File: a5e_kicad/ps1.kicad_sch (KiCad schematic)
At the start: 59 parts, among them U1201 MPM54304GMN-0000, U1303 MPM3810AGQB

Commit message: add vias to lppdr balls
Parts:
- renumbered C1212 to C157, C1208 to C158, C1209 to C159, C1362 to C160, C1211 to C161, C1361 to C162, C1210 to C163, C1213 to C164, C1214 to C165, C1360 to C166, C1215 to C167, C1359 to C168, C1216 to C169, C1363 to C170, C1364 to C171, C1365 to C172, C1366 to C173, C1367 to C174, C1368 to C175, C1369 to C176, C1370 to C177, C1371 to C178, C1372 to C179, C1373 to C180, C1374 to C181, C1375 to C182, C1376 to C183, C1377 to C184, C1378 to C185, C1379 to C186, C1380 to C187, C1381 to C188, C1382 to C189, C1383 to C190, C1384 to C191, C1385 to C192, C1386 to C193, C1387 to C194, C1388 to C195, C1389 to C196, C1390 to C197, R1312 to R64, R1311 to R65, R1308 to R66, R1307 to R67, R1309 to R68, R1310 to R69, R1216 to R70, R1208 to R71, R1209 to R72, R1210 to R73, R1211 to R74, R1313 to R75, R1212 to R76, R1213 to R77, R1214 to R78, R1215 to R79, U1201 to U16, U1303 to U17

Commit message: add comments
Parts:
- added U18, U19, U8: AP61202Z6, Package_TO_SOT_SMD:SOT-563, symbol Regulator_Switching:AP61202Z6

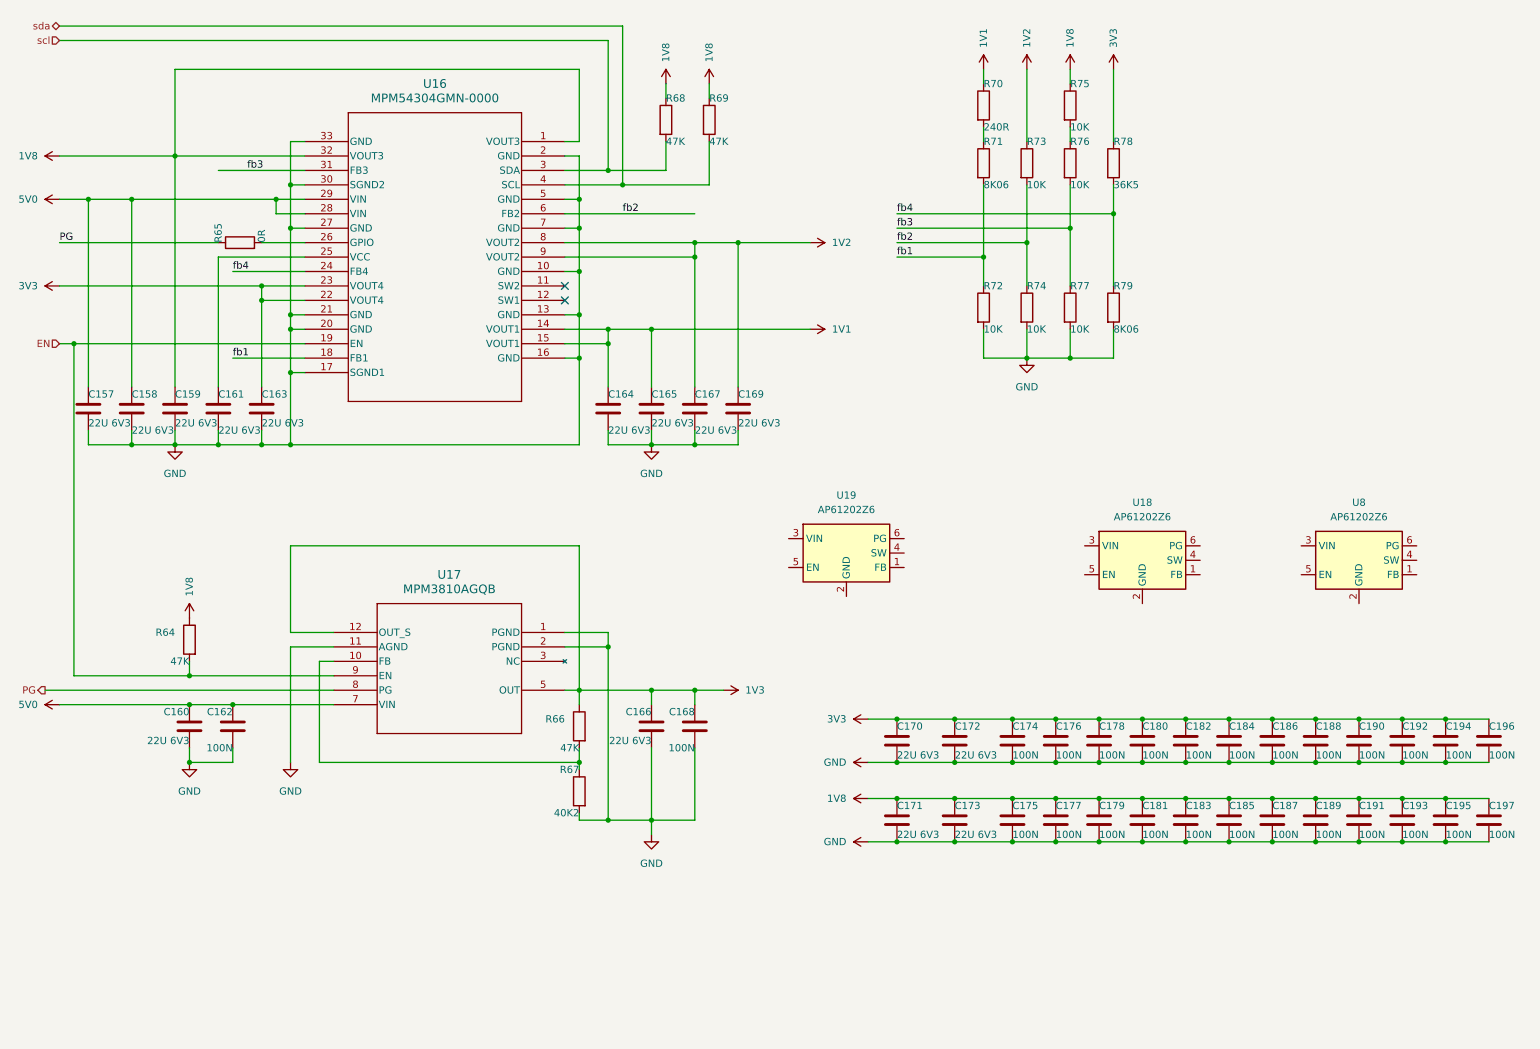
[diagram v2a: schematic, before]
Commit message: start routing power supplies
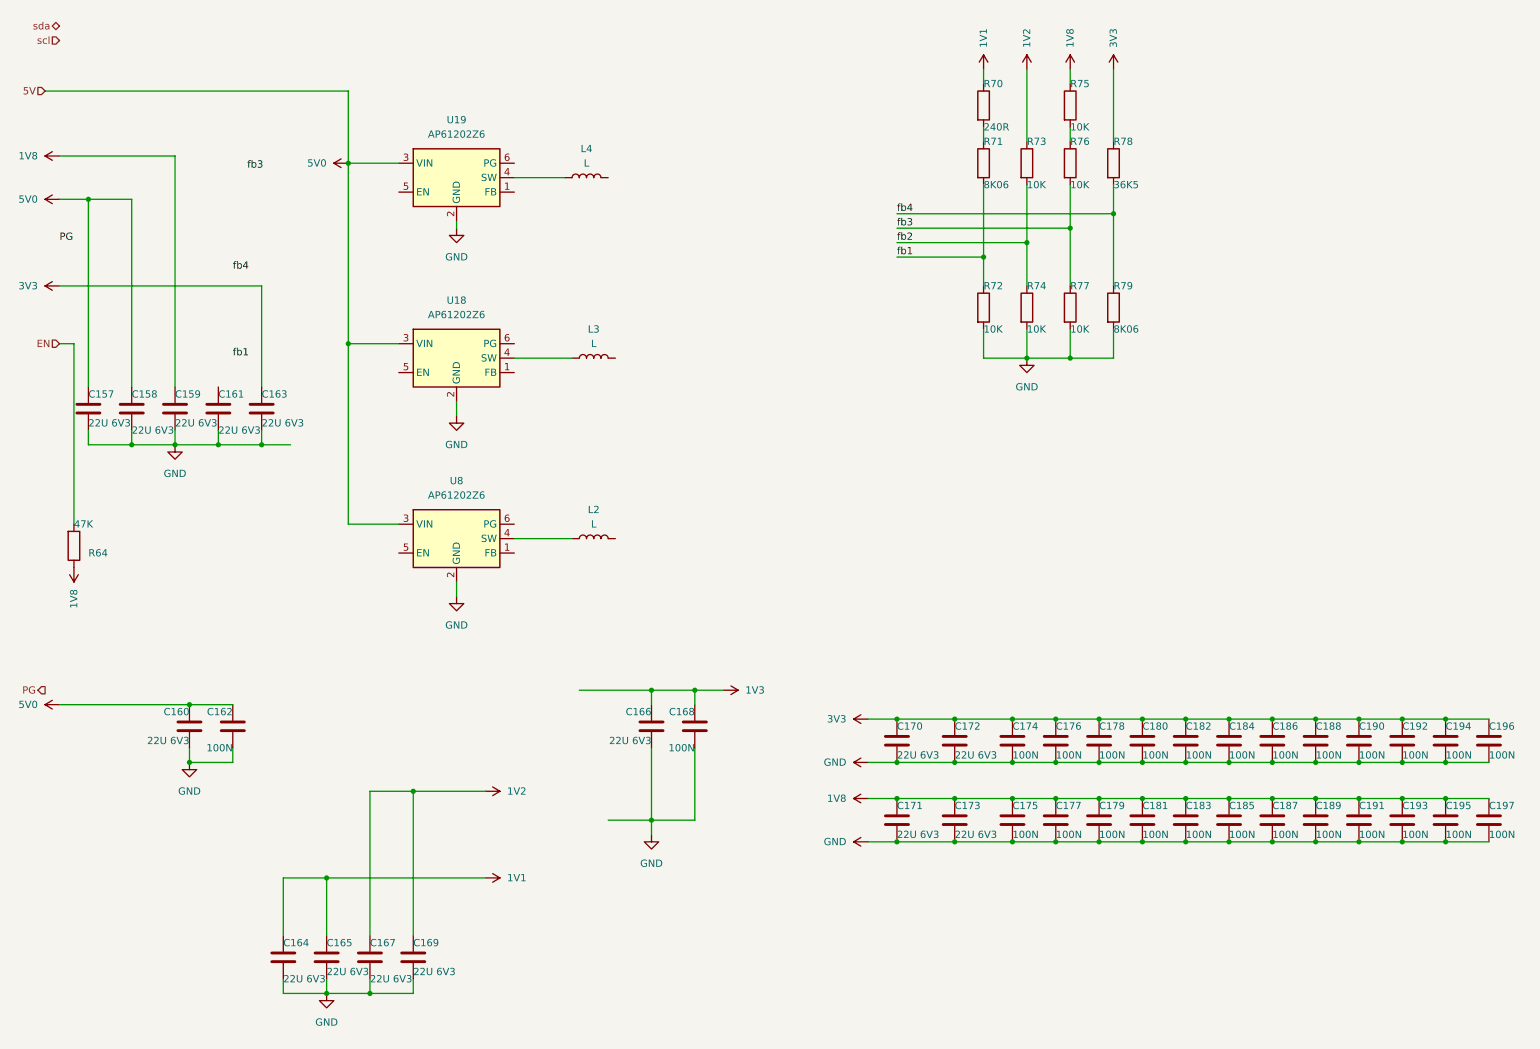
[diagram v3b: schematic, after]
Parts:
- removed R65: 0R, Resistor_SMD:R_0402_1005Metric, symbol Device:R
- removed R66, R68, R69: 47K, Resistor_SMD:R_0402_1005Metric, symbol Device:R
- removed R67: 40K2, Resistor_SMD:R_0402_1005Metric, symbol Device:R
- removed U16: MPM54304GMN-0000, symbol MPM54304GMN:MPM54304GMN-0000
- removed U17: MPM3810AGQB, symbol QFN-12_MPM3810_MNP:MPM3810AGQB
- added L2, L3, L4: L, Inductor_SMD:L_0805_2012Metric, symbol Device:L
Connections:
- net 5V0: now also U18.3 (VIN), U19.3 (VIN), U8.3 (VIN)
- net GND: now also U18.2 (GND), U19.2 (GND), U8.2 (GND)
- net at U19.4 (SW): now also L4.1
- net at U8.4 (SW): now also L2.1
- net at U18.4 (SW): now also L3.1
- no-connect marks 2 -> 0
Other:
- moved on the sheet: C164, C165, C167, C169, R64, U18, U19, U8

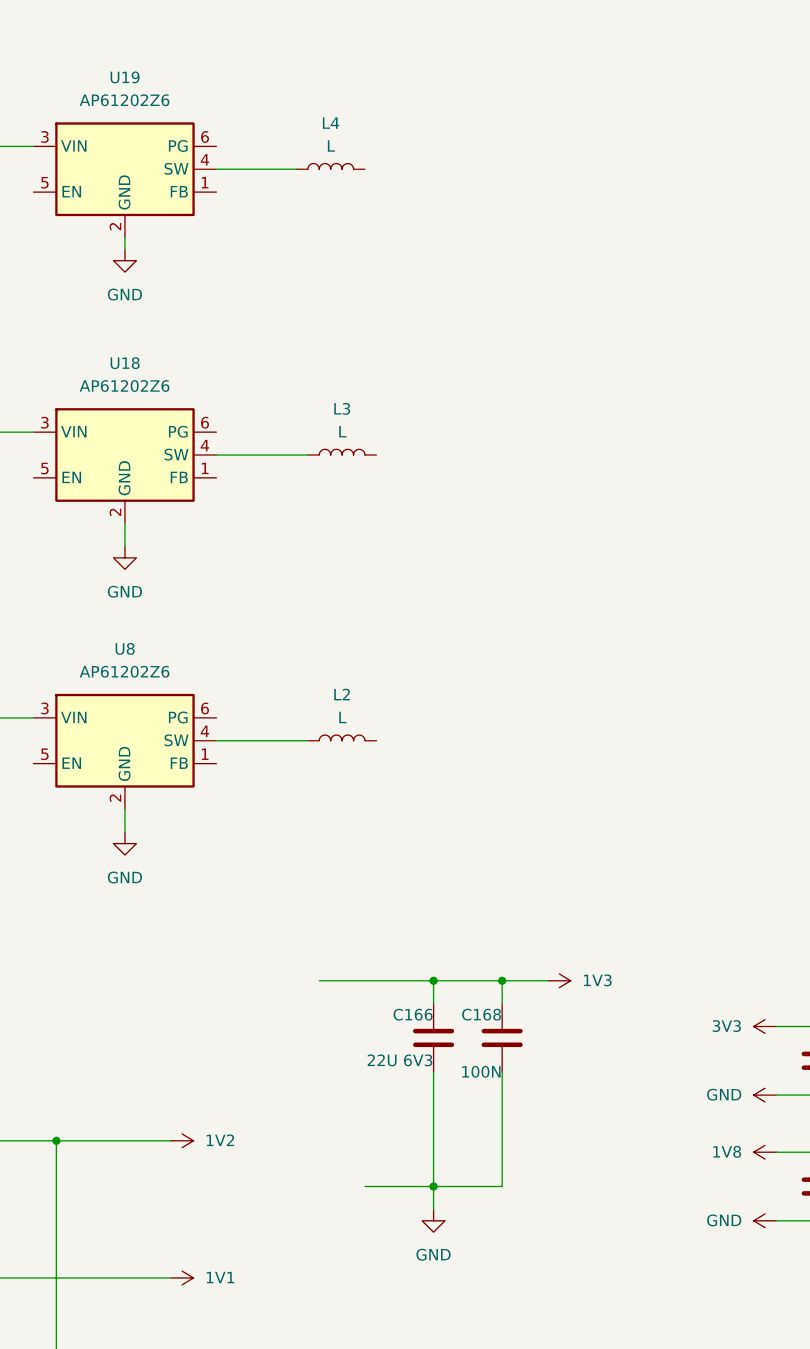
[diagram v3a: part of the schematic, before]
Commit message: sketch length matching for lpddr4
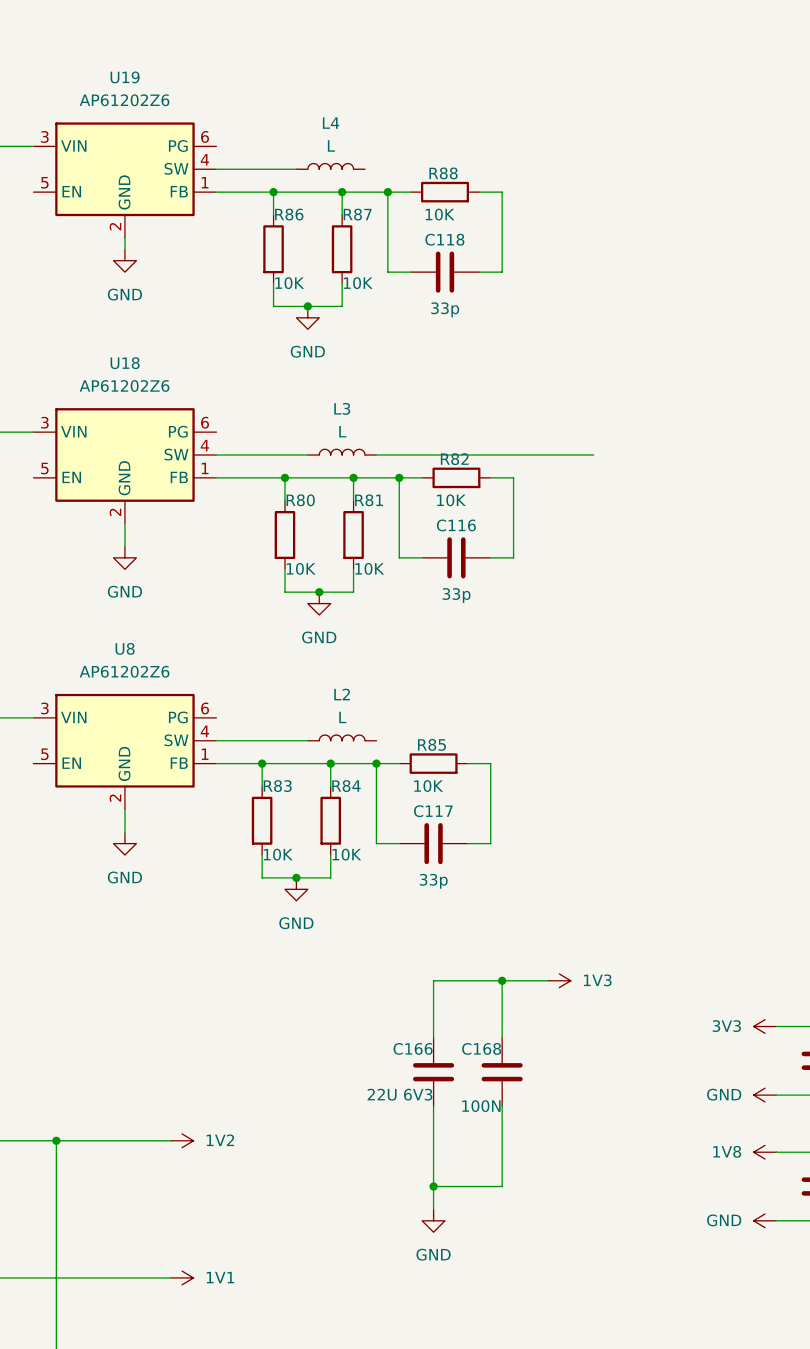
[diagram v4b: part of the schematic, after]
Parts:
- added C116, C117, C118: 33p, Capacitor_SMD:C_0402_1005Metric, symbol Device:C
- added R80, R81, R82, R83, R84, R85, R86, R87, R88: 10K, Resistor_SMD:R_0402_1005Metric, symbol Device:R
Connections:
- net GND: now also R80.2, R81.2, R83.2, R84.2, R86.2, R87.2
- net at U19.1 (FB): now also C118.1, R86.1, R87.1, R88.1
- net at U8.1 (FB): now also C117.1, R83.1, R84.1, R85.1
- net at U18.1 (FB): now also C116.1, R80.1, R81.1, R82.1
- new net: C117.2, R85.2
- new net: C118.2, R88.2
- new net: C116.2, R82.2
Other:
- moved on the sheet: C166, C168

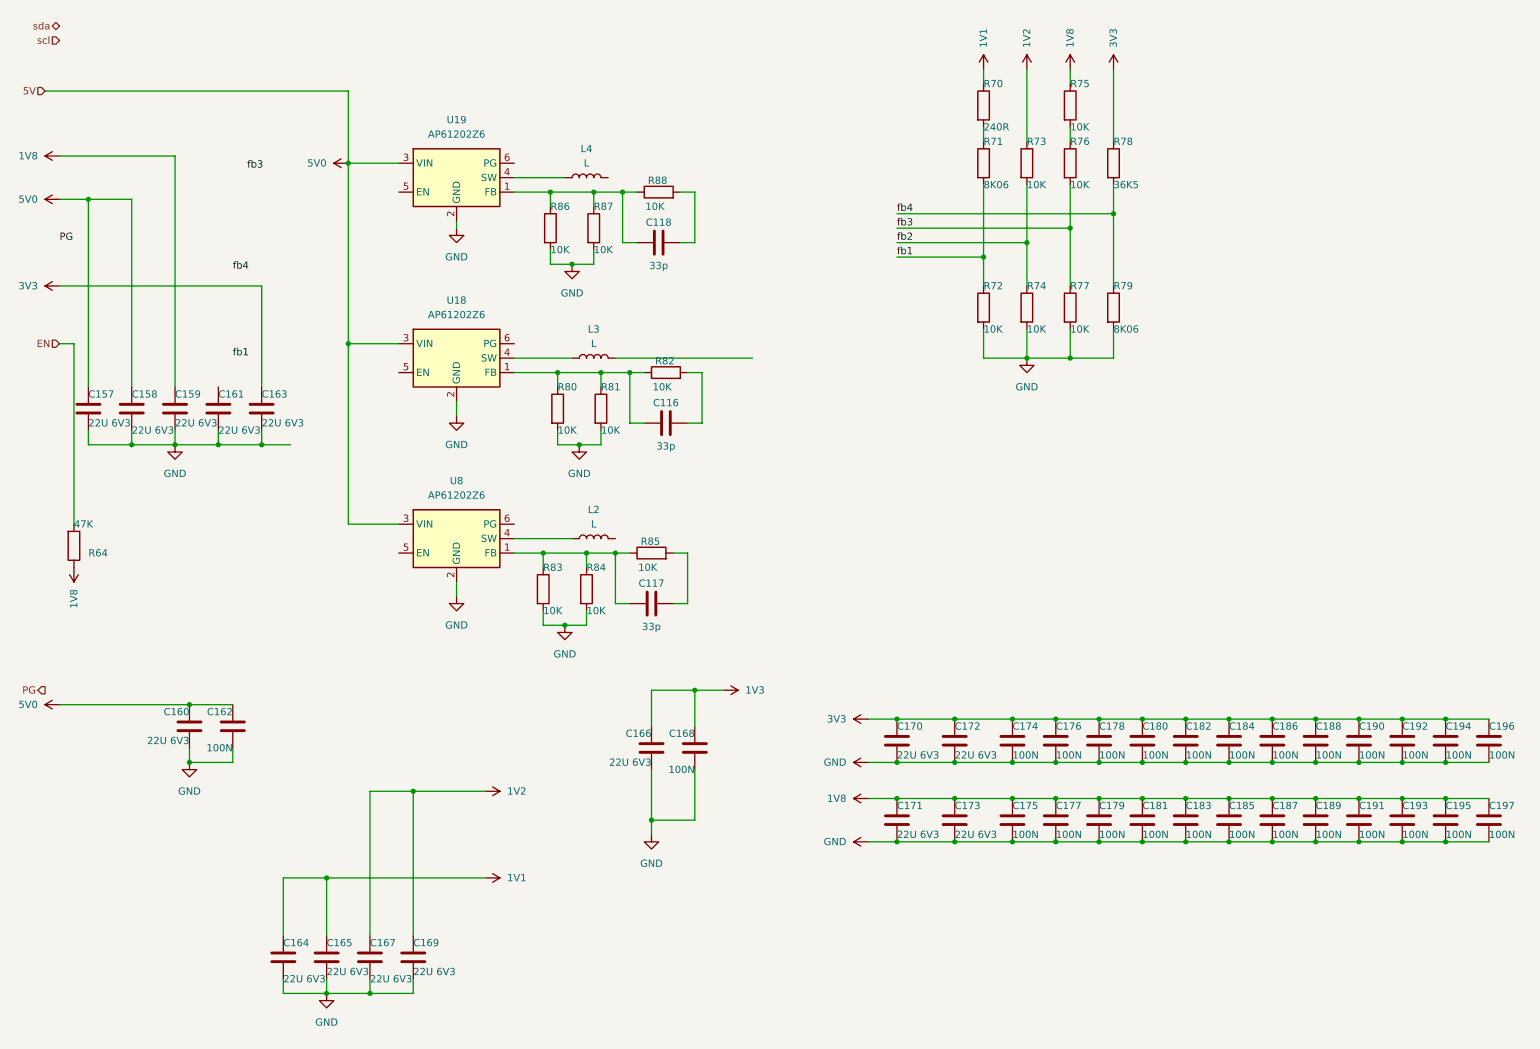
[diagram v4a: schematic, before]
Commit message: add another powersupply for lpddr4
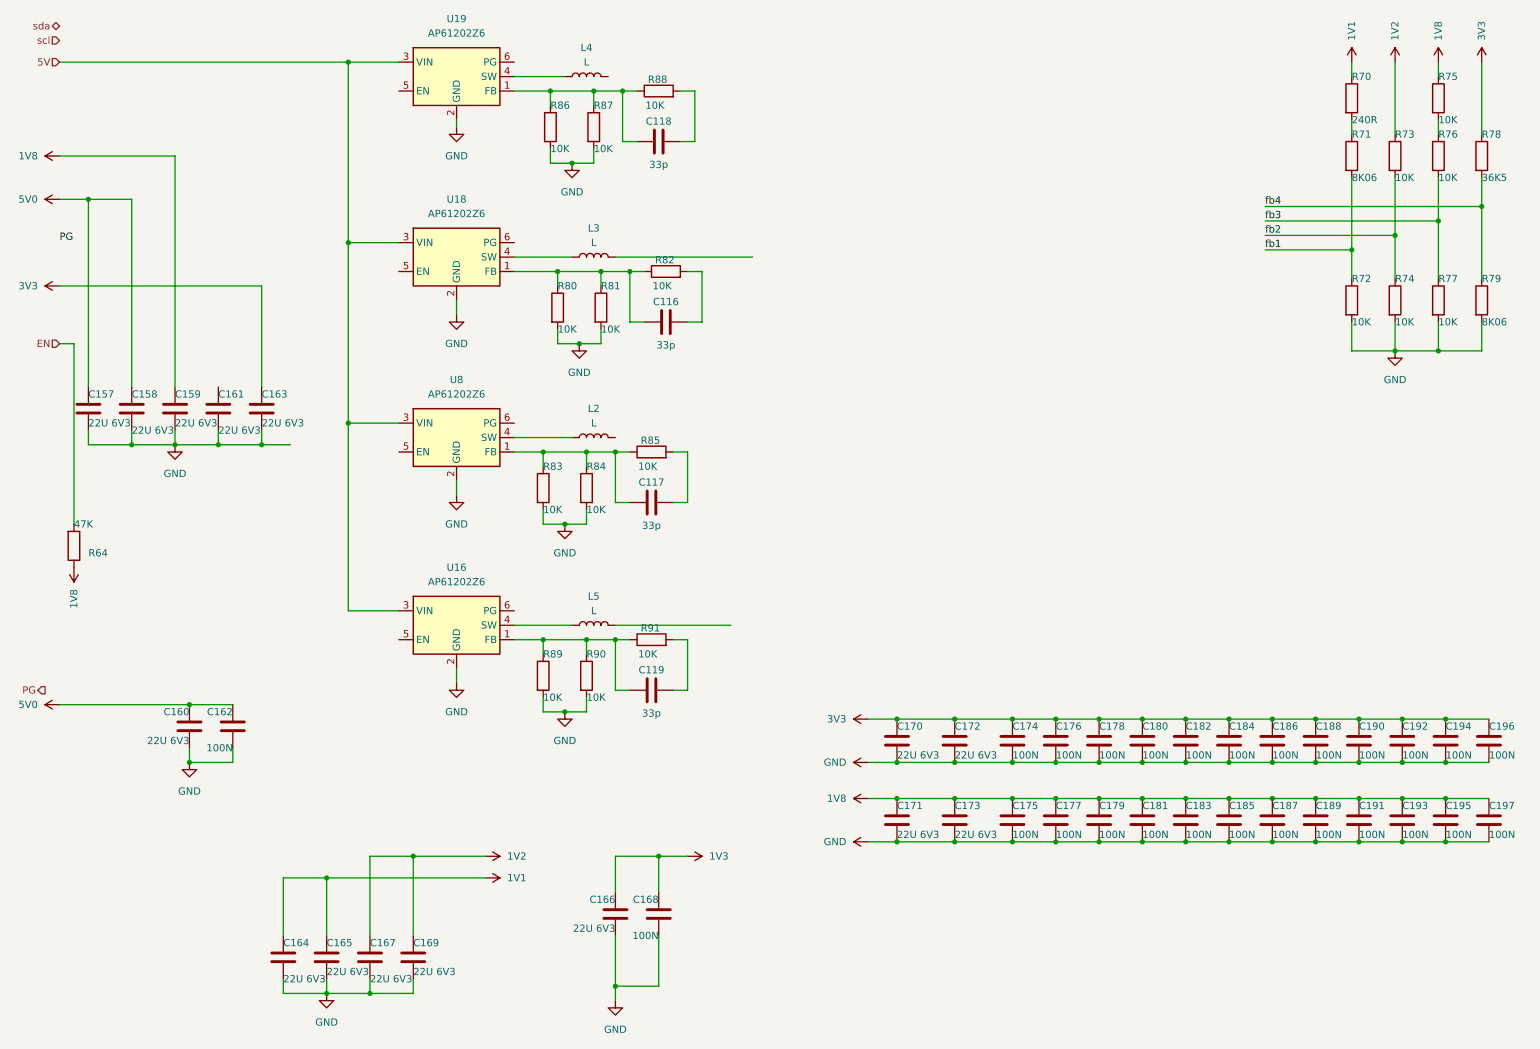
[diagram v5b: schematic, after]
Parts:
- added C119: 33p, Capacitor_SMD:C_0402_1005Metric, symbol Device:C
- added L5: L, Inductor_SMD:L_0805_2012Metric, symbol Device:L
- added R89, R90, R91: 10K, Resistor_SMD:R_0402_1005Metric, symbol Device:R
- added U16: AP61202Z6, Package_TO_SOT_SMD:SOT-563, symbol Regulator_Switching:AP61202Z6
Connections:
- net 5V0: no longer U18.3 (VIN), U19.3 (VIN), U8.3 (VIN)
- net GND: now also R89.2, R90.2, U16.2 (GND)
- new net: C119.1, R89.1, R90.1, R91.1, U16.1 (FB)
- new net: C119.2, R91.2
- new net: L5.1, U16.4 (SW)
- new net 5V: U16.3 (VIN), U18.3 (VIN), U19.3 (VIN), U8.3 (VIN)
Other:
- moved on the sheet: C116, C117, C118, C166, C168, L2, L3, L4, R70, R71, R72, R73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

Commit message: add routes for power supplies
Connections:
- net 1V1: now also C119.2, L5.2, R91.2
- net 3V3: now also C117.2, L2.2, R85.2
- net at C118.2, R88.2: now also L4.2
- net at C116.2, R82.2: now also L3.2

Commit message: savegame, after fixing wird problems with schematic sync
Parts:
- removed C161, C166: 22U 6V3, Capacitor_SMD:C_0402_1005Metric, symbol Device:C
- removed C168: 100N, Capacitor_SMD:C_0402_1005Metric, symbol Device:C
- removed R70: 240R, Resistor_SMD:R_0402_1005Metric, symbol Device:R
- removed R71, R79: 8K06, Resistor_SMD:R_0402_1005Metric, symbol Device:R
- removed R72, R73, R74, R75, R76, R77: 10K, Resistor_SMD:R_0402_1005Metric, symbol Device:R
- removed R78: 36K5, Resistor_SMD:R_0402_1005Metric, symbol Device:R
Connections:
- net 1V2: now also C118.2, L4.2, R88.2
- net 1V8: now also C116.2, L3.2, R82.2
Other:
- moved on the sheet: C119, L5, R89, R90, R91, U16

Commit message: more fiddling with aux power supplies
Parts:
- added C203, C204, C205: 22U 6V3, Capacitor_SMD:C_0402_1005Metric, symbol Device:C
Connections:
- net 1V2: now also C203.1, C204.1
- net GND: now also C203.2, C204.2, C205.2
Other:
- moved on the sheet: C164, C165, C167
